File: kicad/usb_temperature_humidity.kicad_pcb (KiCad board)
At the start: 2 copper layers, 72 x 47.5 mm, 14 parts, among them SW1 SW_SPDT, SW2 SW_SPDT, U1 SeeeduinoXIAO, U2 SHT-31, U3 PinHeader_XIAO, U4 PinHeader_XIAO

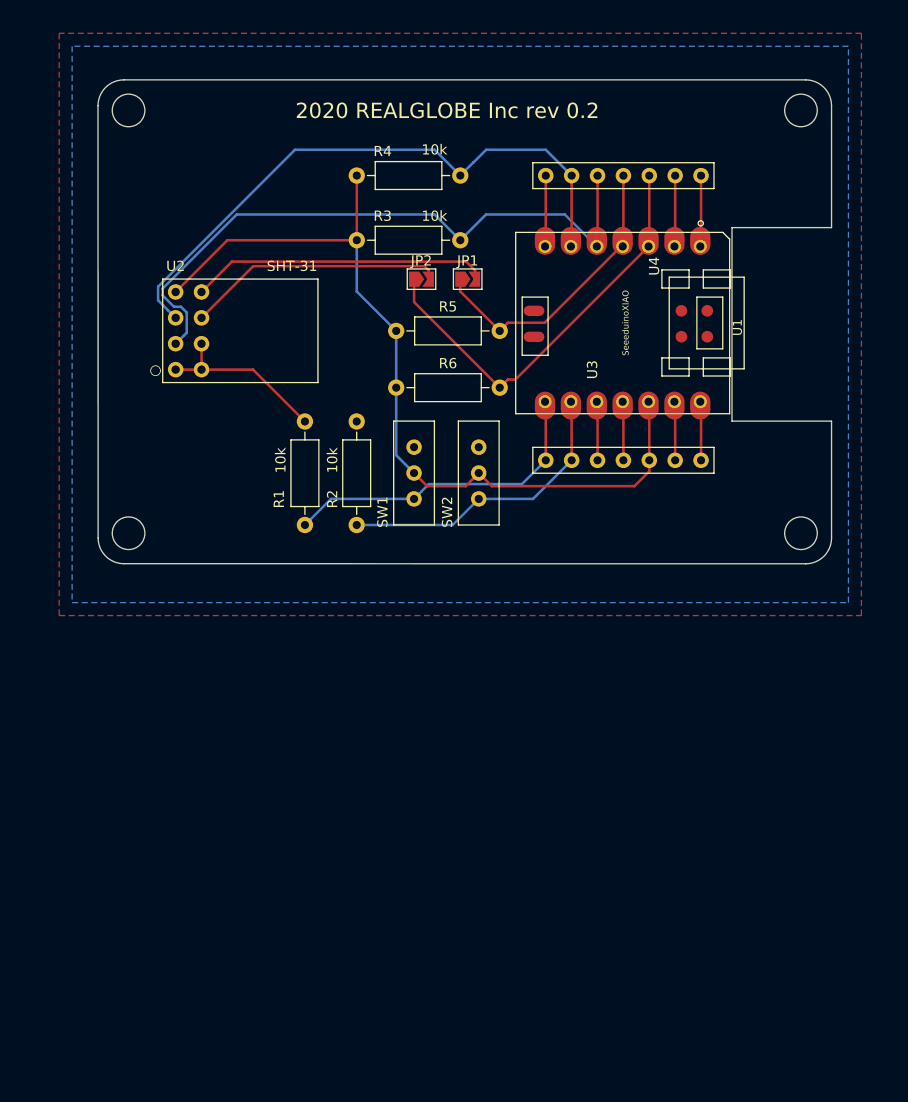
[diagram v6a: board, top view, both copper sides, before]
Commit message: シンボルをaliexpressのSHT-31に置き換えた
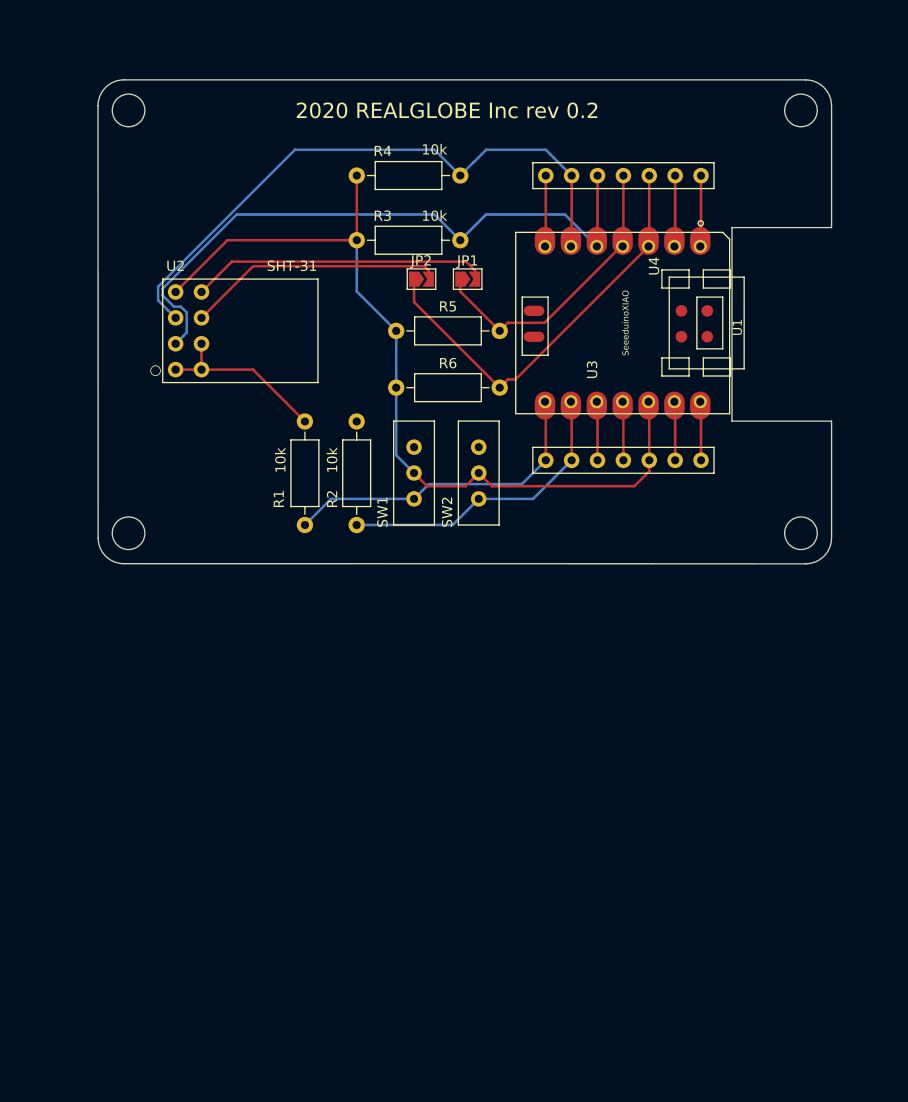
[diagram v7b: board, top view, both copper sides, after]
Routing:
- removed copper zone on B.Cu, net GND
- removed copper zone on F.Cu, net GND
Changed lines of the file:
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@@
   (segment (start 43.95 -31.76906) (end 43.87782 -31.69688) (width 0.25) (layer F.Cu) (net 18))
   (segment (start 43.95 -38.1) (end 43.95 -31.76906) (width 0.25) (layer F.Cu) (net 18))
-  (segment (start 51.57 -31.76906) (end 51.49782 -31.69688) (width 0.25) (layer F.Cu) (net 21))
-  (segment (start 51.57 -38.1) (end 51.57 -31.76906) (width 0.25) (layer F.Cu) (net 21))
-  (segment (start 54.11 -31.76906) (end 54.03782 -31.69688) (width 0.25) (layer F.Cu) (net 23))
-  (segment (start 54.11 -38.1) (end 54.11 -31.76906) (width 0.25) (layer F.Cu) (net 23))
   (segment (start 56.65 -31.76906) (end 56.57782 -31.69688) (width 0.25) (layer F.Cu) (net 19))
   (segment (start 56.65 -38.1) (end 56.65 -31.76906) (width 0.25) (layer F.Cu) (net 19))
   (segment (start 59.19 -31.76906) (end 59.11782 -31.69688) (width 0.25) (layer F.Cu) (net 20))
   (segment (start 59.19 -38.1) (end 59.19 -31.76906) (width 0.25) (layer F.Cu) (net 20))
+  (segment (start 51.57 -31.76906) (end 51.49782 -31.69688) (width 0.25) (layer F.Cu) (net 21))
+  (segment (start 51.57 -38.1) (end 51.57 -31.76906) (width 0.25) (layer F.Cu) (net 21))
   (segment (start 35.56 -26.73) (end 39.43 -22.86) (width 0.25) (layer F.Cu) (net 21))
   (segment (start 35.56 -27.94) (end 35.56 -26.73) (width 0.25) (layer F.Cu) (net 21))
@@
   (segment (start 13.14001 -29.66001) (end 36.13999 -29.66001) (width 0.25) (layer F.Cu) (net 22))
   (segment (start 10.16 -26.68) (end 13.14001 -29.66001) (width 0.25) (layer F.Cu) (net 22))
+  (segment (start 54.11 -31.76906) (end 54.03782 -31.69688) (width 0.25) (layer F.Cu) (net 23))
+  (segment (start 54.11 -38.1) (end 54.11 -31.76906) (width 0.25) (layer F.Cu) (net 23))
   (segment (start 31.025 -25.695) (end 39.43 -17.29) (width 0.25) (layer F.Cu) (net 23))
   (segment (start 31.025 -27.94) (end 31.025 -25.695) (width 0.25) (layer F.Cu) (net 23))
@@
       )
     )
-  )
-  (zone (net 1) (net_name GND) (layer B.Cu) (hatch edge 0.508)
-    (connect_pads (clearance 0.508))
-    (min_thickness 0.254)
-    (fill yes (arc_segments 32) (thermal_gap 0.508) (thermal_bridge_width 0.508))
-    (polygon
-      (pts
-        (xy 73.66 -50.8) (xy -2.54 -50.8) (xy -2.54 3.81) (xy 73.66 3.81)
-      )
-    )
-  )
-  (zone (net 1) (net_name GND) (layer F.Cu) (hatch edge 0.508)
-    (connect_pads (clearance 0.508))
-    (min_thickness 0.254)
-    (fill yes (arc_segments 32) (thermal_gap 0.508) (thermal_bridge_width 0.508))
-    (polygon
-      (pts
-        (xy 74.93 -52.07) (xy -3.81 -52.07) (xy -3.81 5.08) (xy 74.93 5.08)
-      )
-    )

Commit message: 配線済みDRC ok
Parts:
- added U5: SHT-31_aliexpress, kicad_mylib:SHT-31_aliexpress, F.Cu at (3.81, -19.1)
- moved U2 1.79 mm to (7.62, -19.1)
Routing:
- net Net-(R4-Pad2): track 59.5 -> 72.8 mm
- net GND: track 22.7 -> 28.7 mm
- net +3V3: track 83.2 -> 87.8 mm
- net Net-(JP2-Pad2): track 25.4 -> 23.6 mm
- net Net-(JP1-Pad2): track 29.3 -> 27.5 mm
- net Net-(R3-Pad2): track 62.7 -> 61.9 mm
- added copper zone on B.Cu, net GND
- added copper zone on F.Cu, net GND
